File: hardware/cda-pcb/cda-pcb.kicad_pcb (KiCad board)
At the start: 4 copper layers, 112 x 127 mm, 190 parts, among them J1 ICD15S13E4GX00LF, J2 ICD15S13E4GX00LF, J3 ICD15S13E4GX00LF, J4 ICD15S13E4GX00LF, J6 Conn_01x06, P1 0022272021, U1 ADS124S08IRHBT, U10 SN74AHCT125RGYR, U2 ADS124S08IRHBT, U3 ADS124S08IRHBT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

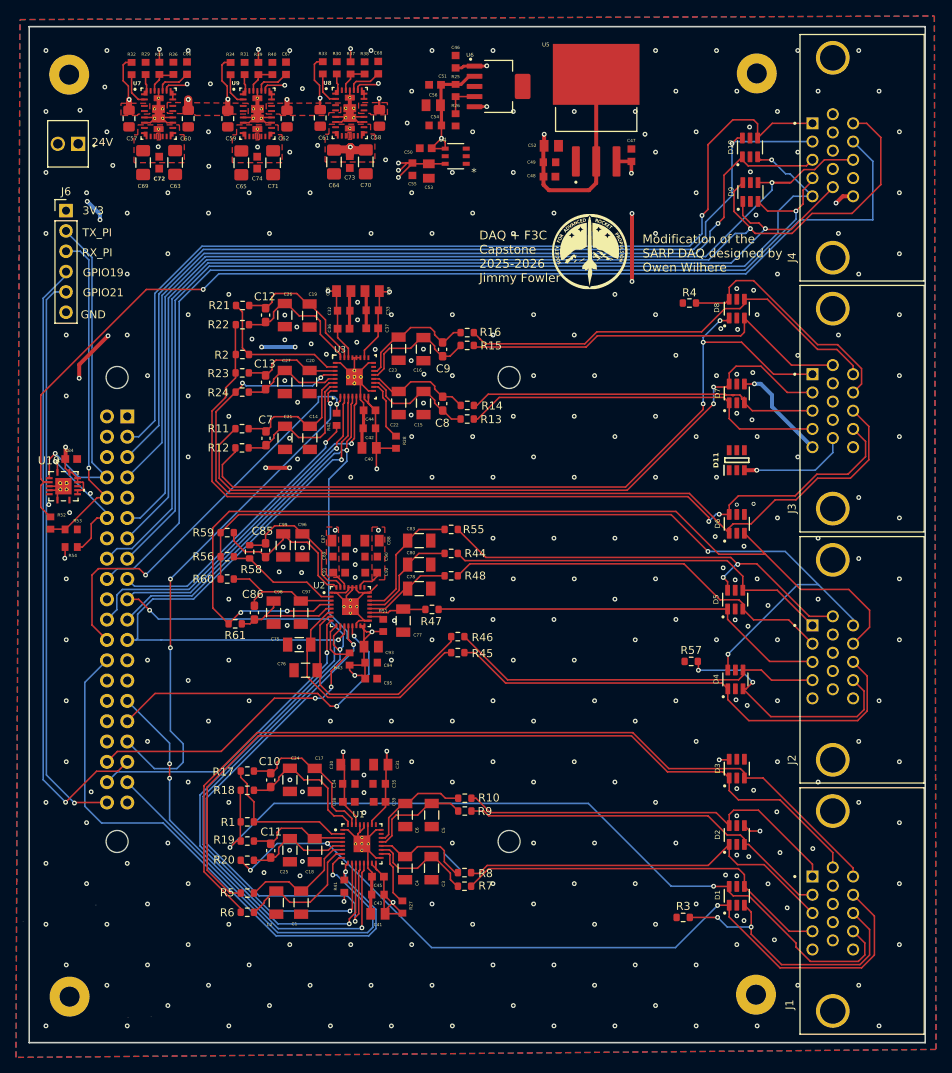
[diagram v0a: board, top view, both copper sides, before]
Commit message: added ESD protection to daughterboard & fiducials
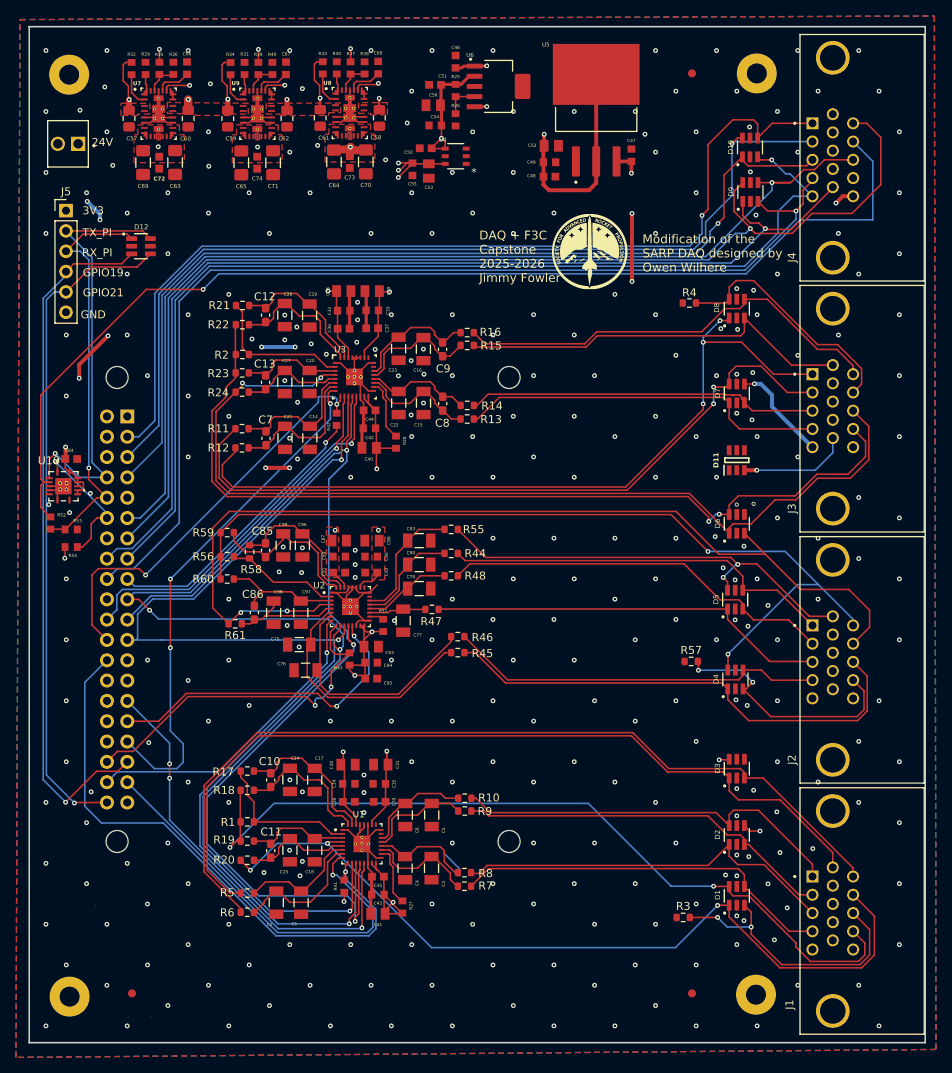
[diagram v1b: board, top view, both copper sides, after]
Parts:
- added D12: ESDA6V1BC6, ESDA6V1BC6:SOT95P280X145-6N, F.Cu at (80.3, 60.1)
- added REF**: Fiducial_1mm_Mask3mm, Fiducial:Fiducial_1mm_Mask3mm, F.Cu at (149.2, 153.5)
- added REF**: Fiducial_1mm_Mask3mm, Fiducial:Fiducial_1mm_Mask3mm, F.Cu at (79.2, 153.5)
- added REF**: Fiducial_1mm_Mask3mm, Fiducial:Fiducial_1mm_Mask3mm, F.Cu at (149.2, 38.5)
- renumbered J6 to J5
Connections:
- U7 pad 32: GND -> (no net)
- U7 pad 35: GND -> (no net)
- U7 pad 36: GND -> (no net)
- U8 pad 31: +11V -> (no net)
- U8 pad 32: GND -> (no net)
- U8 pad 35: GND -> (no net)
- U8 pad 36: GND -> (no net)
- U9 pad 31: +6V -> (no net)
- U9 pad 32: GND -> (no net)
- U9 pad 35: GND -> (no net)
- U9 pad 36: GND -> (no net)
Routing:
- net /GPIO21: track 71.3 -> 83.8 mm
- net /TX_PI: track 44.3 -> 55.3 mm
- net /RX_PI: track 42.7 -> 52.0 mm
- net /GPIO19: track 78.5 -> 87.6 mm
- net /CE3: track 43.3 -> 44.6 mm

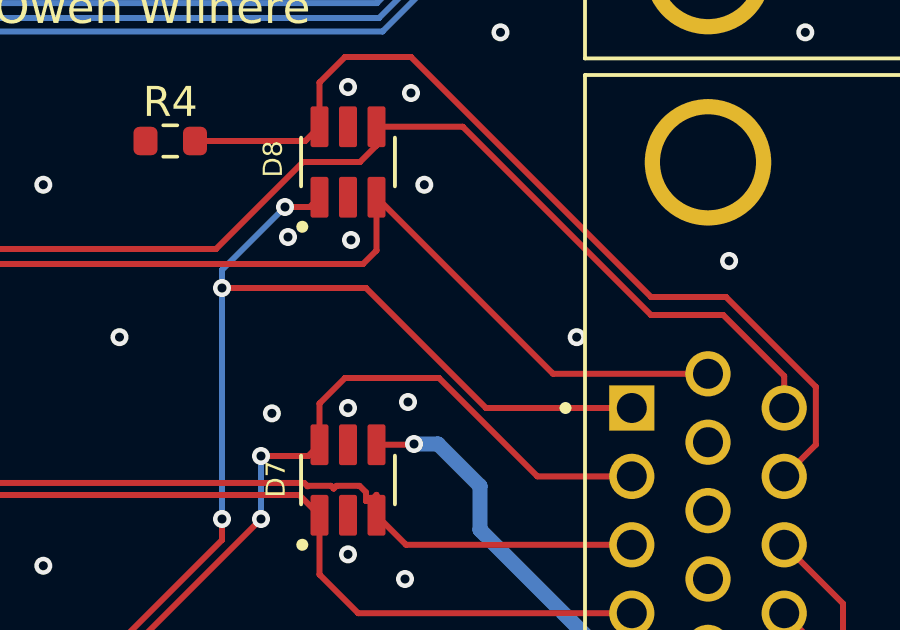
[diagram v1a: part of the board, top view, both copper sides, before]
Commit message: add fiducials, remove handsoldered footprints, added indicator LEDs
Add board backups and make multiple PCB/schematic edits: adjust fiducial positions, add a new via, and tweak component and label coordinates for alignment. Add several schematic symbols and instances (LEDs, +5V/+9V/+10V power symbols, resistors R49/R63) and numerous small wire segments to connect indicators. Update footprints for several capacitors/inductors/ICs and simplify some footprint names. Also change KiCad project preference (high_contrast_mode) and apply general cleanup/positioning adjustments across cda-pcb.kicad_pcb and cda-pcb.kicad_sch.
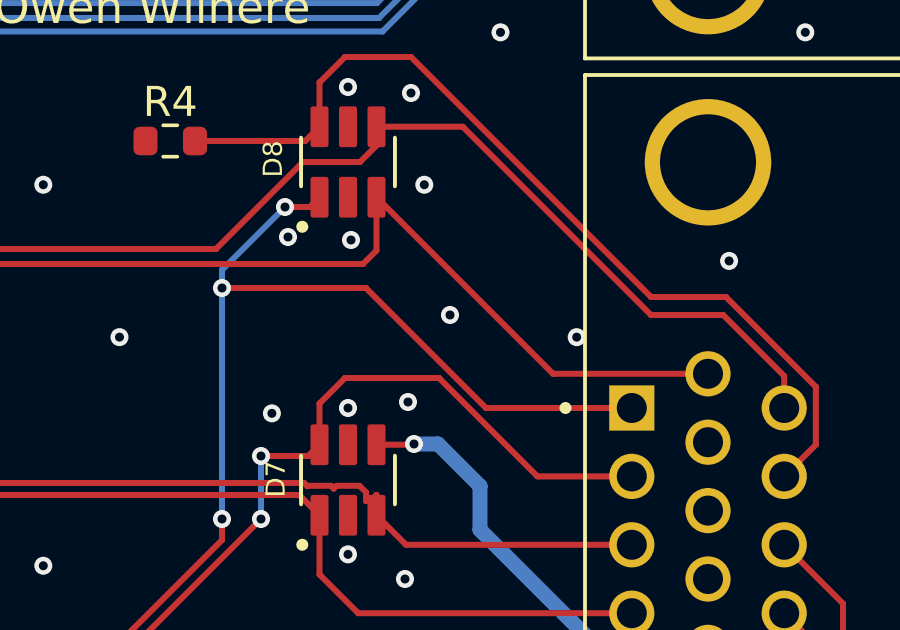
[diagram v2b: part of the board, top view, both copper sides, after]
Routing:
- net GND: vias 313 -> 314
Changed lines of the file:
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@@
 		)
 		(property "Value" "Fiducial_1mm_Mask3mm"
-			(at 0 2.45 0)
+			(at -3 2.45 0)
 			(layer "F.Fab")
 			(effects
@@
 		)
 		(property "Value" "Fiducial_1mm_Mask3mm"
-			(at 0 2.45 0)
+			(at 4 2.45 0)
 			(layer "F.Fab")
 			(effects
@@
 		)
 		(property "Value" "Fiducial_1mm_Mask3mm"
-			(at 0 2.45 0)
+			(at 3 -3 0)
 			(layer "F.Fab")
 			(effects
@@
 		(size 0.6)
 		(drill 0.3)
+		(layers "F.Cu" "B.Cu")
+		(free yes)
+		(net 2)
+	)
+	(via
+		(at 158.174699 72.987691)
+		(size 0.6)
+		(drill 0.3)

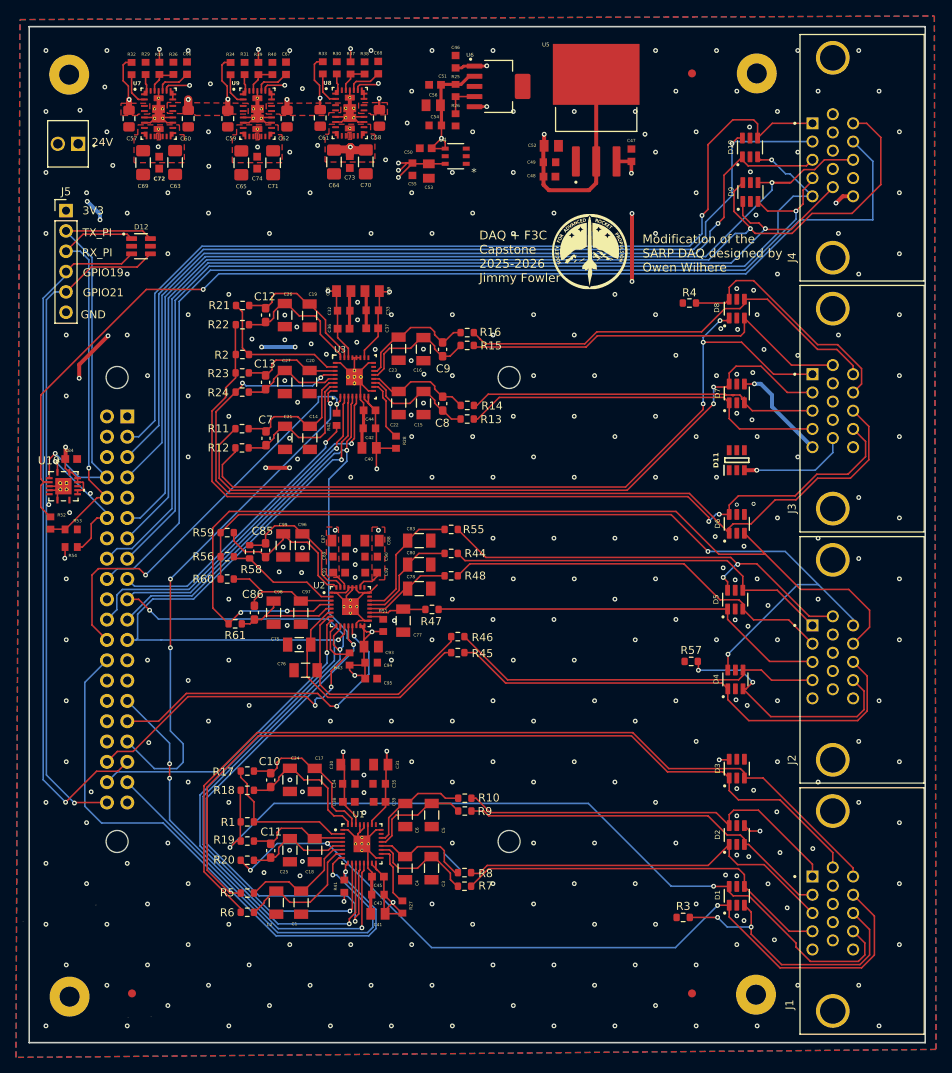
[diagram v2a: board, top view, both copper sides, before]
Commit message: added some little guys
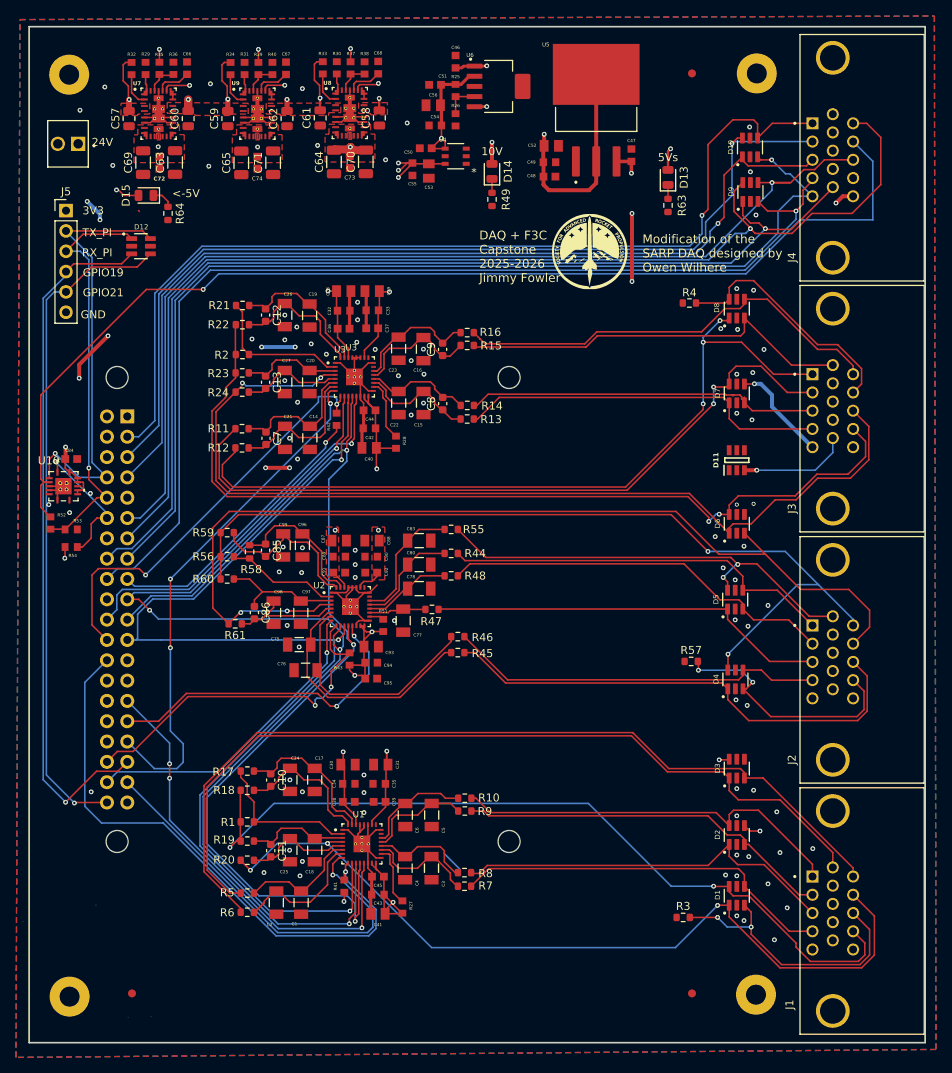
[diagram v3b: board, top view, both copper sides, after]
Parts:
- removed the G*** at (80.1, 153.2)
- added D13: LED, LED_SMD:LED_0805_2012Metric, F.Cu at (146.2, 51.5)
- added D14: LED, LED_SMD:LED_0805_2012Metric, F.Cu at (124.2, 50.7)
- added D15: LED, LED_SMD:LED_0805_2012Metric, F.Cu at (80.9, 53.7)
- added G***: LOGO, LOGO, B.Cu at (87.3, 150.6)
- added G***: LOGO, LOGO, B.Cu at (140.5, 139.9)
- added G***: LOGO, LOGO, B.Cu at (101.3, 150.7)
- added R49: 5.6k, Resistor_SMD:R_0603_1608Metric, F.Cu at (124.2, 54.2)
- added R63: 1.8k, Resistor_SMD:R_0603_1608Metric, F.Cu at (146.2, 55.0)
- added R64: 1.8k, Resistor_SMD:R_0603_1608Metric, F.Cu at (83.7, 56.0)
- C10, C11, C12, C13, C7, C8, C85, C86, C9: footprint Capacitor_SMD:C_0603_1608Metric_Pad1.08x0.95mm_HandSolder -> Capacitor_SMD:C_0603_1608Metric
- C57, C58, C59, C60, C61, C62: footprint Capacitor_SMD:C_0805_2012Metric_Pad1.18x1.45mm_HandSolder -> Capacitor_SMD:C_0805_2012Metric
- C63, C64, C65, C69, C70, C71: footprint Inductor_SMD:L_1206_3216Metric_Pad1.42x1.75mm_HandSolder -> Capacitor_SMD:C_1206_3216Metric
- U3: footprint footprintsADC:RHB0032M -> ADS124S08IRHBT:QFN50P500X500X100-33N
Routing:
- net +5V: track 65.3 -> 68.5 mm, vias 3 -> 4
- net Net-(D15-K): track 0.00 -> 2.80 mm
- net +5Vs: track 477.0 -> 479.8 mm
- net +10Vs: track 102.2 -> 104.9 mm, vias 4 -> 5
- net Net-(D14-K): track 0.00 -> 1.74 mm
- net Net-(D13-K): track 0.00 -> 1.74 mm
- net GND: track 110.9 -> 111.1 mm, vias 314 -> 90
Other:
- board text added: "10V"
- board text added: "5Vs"
- board text added: "<-5V"
- board text added: "Controls & Electronics Team: Elyse Lian, Grace Lovell, Jimmy Fowler, Keira Morrisey, Prabhav Rawat"
